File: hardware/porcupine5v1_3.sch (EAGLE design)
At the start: 45 parts, among them X1 PROGCON

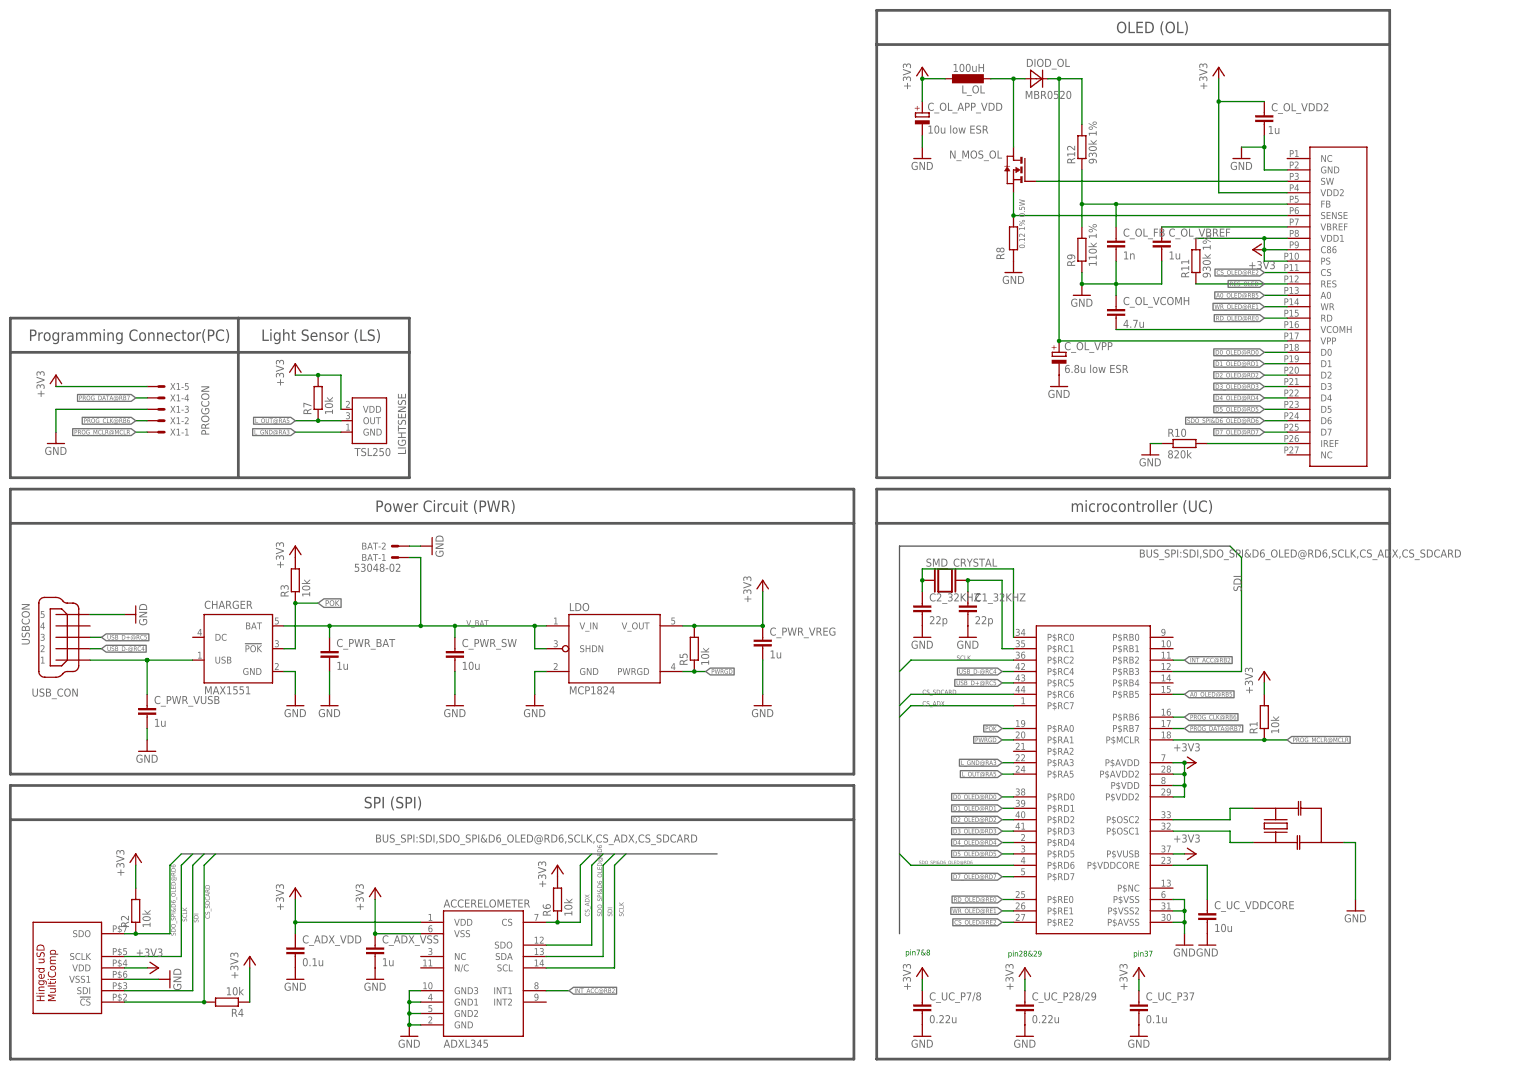
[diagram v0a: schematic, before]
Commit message: OLED version update wiring
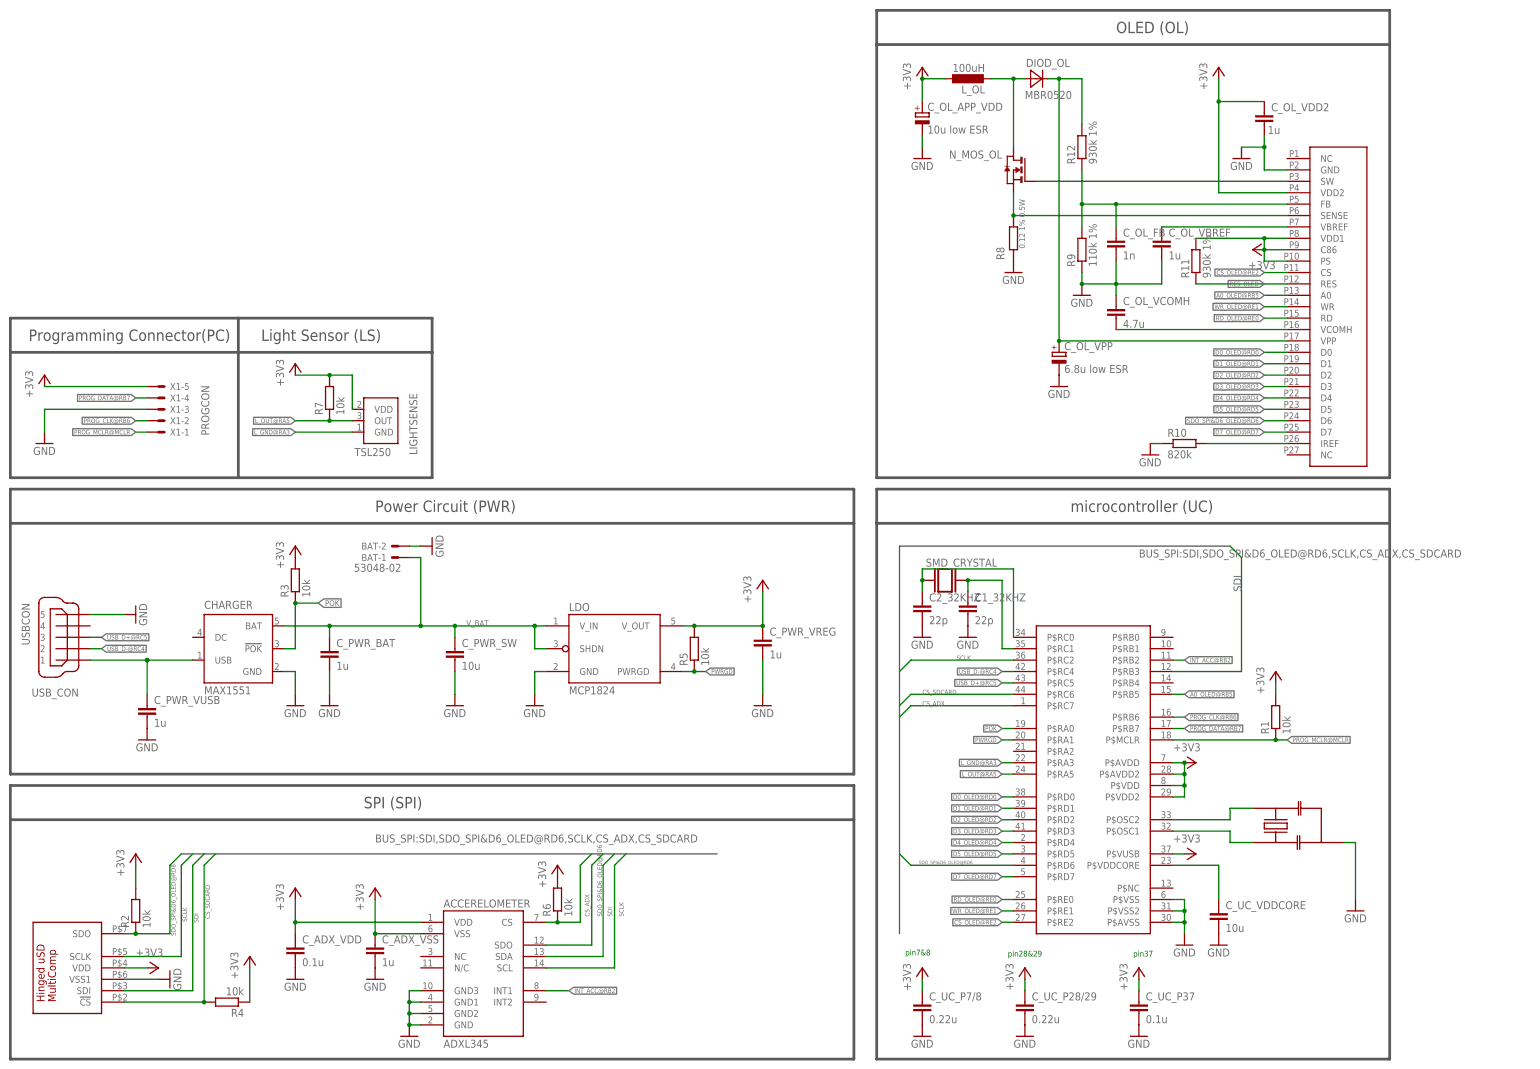
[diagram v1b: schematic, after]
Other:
- moved on the sheet: C_UC_VDDCORE, LIGHTSENSE, R1, R7
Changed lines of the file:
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@@
 <wire x1="5.08" y1="132.08" x2="55.88" y2="132.08" width="0.6096" layer="97"/>
 <wire x1="55.88" y1="167.64" x2="5.08" y2="167.64" width="0.6096" layer="97"/>
-<wire x1="55.88" y1="132.08" x2="93.98" y2="132.08" width="0.6096" layer="97"/>
-<wire x1="93.98" y1="132.08" x2="93.98" y2="160.02" width="0.6096" layer="97"/>
-<wire x1="93.98" y1="160.02" x2="93.98" y2="167.64" width="0.6096" layer="97"/>
+<wire x1="55.88" y1="132.08" x2="99.06" y2="132.08" width="0.6096" layer="97"/>
+<wire x1="99.06" y1="132.08" x2="99.06" y2="160.02" width="0.6096" layer="97"/>
+<wire x1="99.06" y1="160.02" x2="99.06" y2="167.64" width="0.6096" layer="97"/>
 <wire x1="55.88" y1="167.64" x2="55.88" y2="132.08" width="0.6096" layer="97"/>
 <wire x1="5.08" y1="121.92" x2="5.08" y2="66.04" width="0.6096" layer="97"/>
@@
 <wire x1="312.42" y1="121.92" x2="312.42" y2="2.54" width="0.6096" layer="97"/>
 <wire x1="312.42" y1="2.54" x2="198.12" y2="2.54" width="0.6096" layer="97"/>
-<wire x1="5.08" y1="160.02" x2="93.98" y2="160.02" width="0.6096" layer="97"/>
-<wire x1="55.88" y1="167.64" x2="93.98" y2="167.64" width="0.6096" layer="97"/>
+<wire x1="5.08" y1="160.02" x2="99.06" y2="160.02" width="0.6096" layer="97"/>
+<wire x1="55.88" y1="167.64" x2="99.06" y2="167.64" width="0.6096" layer="97"/>
 <text x="9.144" y="162.56" size="2.54" layer="97">Programming Connector(PC)</text>
 <text x="204.47" y="25.654" size="1.27" layer="91">pin7&amp;8</text>
@@
 </plain>
 <instances>
-<instance part="GND3" gate="1" x="15.24" y="139.7"/>
+<instance part="GND3" gate="1" x="12.7" y="139.7"/>
 <instance part="SDCARD_CON" gate="G$1" x="30.48" y="25.4" smashed="yes" rot="R90"/>
 <instance part="GND16" gate="1" x="40.64" y="20.32" rot="R90"/>
-<instance part="LIGHTSENSE" gate="G$1" x="88.9" y="137.16" smashed="yes">
-<attribute name="NAME" x="93.218" y="137.16" size="1.778" layer="95" rot="R90"/>
+<instance part="LIGHTSENSE" gate="G$1" x="91.44" y="137.16" smashed="yes">
+<attribute name="NAME" x="95.758" y="137.16" size="1.778" layer="95" rot="R90"/>
 <attribute name="VALUE" x="89.916" y="138.684" size="1.778" layer="96" rot="R180"/>
 </instance>
@@
 <instance part="GND20" gate="1" x="33.02" y="101.6" rot="R90"/>
 <instance part="C_PWR_VUSB" gate="G$1" x="35.56" y="81.28"/>
-<instance part="GND21" gate="1" x="35.56" y="71.12"/>
+<instance part="GND21" gate="1" x="35.56" y="73.66"/>
 <instance part="GND23" gate="1" x="99.06" y="116.84" rot="R90"/>
 <instance part="C_PWR_SW" gate="G$1" x="104.14" y="93.98"/>
@@
 <instance part="+3V7" gate="G$1" x="269.24" y="68.58" rot="R270"/>
 <instance part="GND6" gate="1" x="266.7" y="27.94"/>
-<instance part="GND7" gate="1" x="271.78" y="27.94"/>
+<instance part="GND7" gate="1" x="274.32" y="27.94"/>
 <instance part="C_UC_P7/8" gate="G$1" x="208.28" y="15.24"/>
 <instance part="C_UC_P28/29" gate="G$1" x="231.14" y="15.24"/>
@@
 <instance part="GND13" gate="1" x="208.28" y="7.62"/>
 <instance part="+3V14" gate="G$1" x="68.58" y="157.48"/>
-<instance part="R1" gate="G$1" x="284.48" y="78.74" rot="R90"/>
-<instance part="+3V15" gate="G$1" x="15.24" y="154.94"/>
+<instance part="R1" gate="G$1" x="287.02" y="78.74" rot="R90"/>
+<instance part="+3V15" gate="G$1" x="12.7" y="154.94"/>
 <instance part="+3V13" gate="G$1" x="86.36" y="40.64"/>
-<instance part="+3V16" gate="G$1" x="284.48" y="88.9"/>
+<instance part="+3V16" gate="G$1" x="287.02" y="88.9"/>
 <instance part="R2" gate="G$1" x="33.02" y="35.56" rot="R90"/>
 <instance part="R4" gate="G$1" x="53.34" y="15.24" rot="R180"/>
 <instance part="+3V8" gate="G$1" x="33.02" y="48.26"/>
 <instance part="+3V10" gate="G$1" x="58.42" y="25.4"/>
-<instance part="C_UC_VDDCORE" gate="G$1" x="271.78" y="35.56"/>
+<instance part="C_UC_VDDCORE" gate="G$1" x="274.32" y="35.56"/>
 <instance part="+3V2" gate="G$1" x="38.1" y="22.86" rot="R270"/>
 <instance part="CON_OLED" gate="G$1" x="292.1" y="170.18"/>
@@
 <instance part="BAT" gate="-1" x="91.44" y="114.3" rot="R180"/>
 <instance part="BAT" gate="-2" x="91.44" y="116.84" rot="R180"/>
-<instance part="R7" gate="G$1" x="73.66" y="149.86" rot="R90"/>
+<instance part="R7" gate="G$1" x="76.2" y="149.86" rot="R90"/>
 </instances>
 <busses>
@@
 <net name="GND" class="0">
 <segment>
-<wire x1="35.56" y1="147.32" x2="15.24" y2="147.32" width="0.1524" layer="91"/>
-<wire x1="15.24" y1="147.32" x2="15.24" y2="142.24" width="0.1524" layer="91"/>
+<wire x1="35.56" y1="147.32" x2="12.7" y2="147.32" width="0.1524" layer="91"/>
+<wire x1="12.7" y1="147.32" x2="12.7" y2="142.24" width="0.1524" layer="91"/>
 <pinref part="GND3" gate="1" pin="GND"/>
 <pinref part="X1" gate="-3" pin="S"/>
@@
 </segment>
 <segment>
-<wire x1="35.56" y1="76.2" x2="35.56" y2="73.66" width="0.1524" layer="91"/>
 <pinref part="C_PWR_VUSB" gate="G$1" pin="2"/>
 <pinref part="GND21" gate="1" pin="GND"/>
@@
 <pinref part="LIGHTSENSE" gate="G$1" pin="OUT"/>
 <pinref part="R7" gate="G$1" pin="1"/>
-<wire x1="73.66" y1="144.78" x2="68.58" y2="144.78" width="0.1524" layer="91"/>
-<wire x1="78.74" y1="144.78" x2="73.66" y2="144.78" width="0.1524" layer="91"/>
-<junction x="73.66" y="144.78"/>
+<wire x1="76.2" y1="144.78" x2="68.58" y2="144.78" width="0.1524" layer="91"/>
+<wire x1="81.28" y1="144.78" x2="76.2" y2="144.78" width="0.1524" layer="91"/>
+<junction x="76.2" y="144.78"/>
 </segment>
 <segment>
@@
 </segment>
 <segment>
-<wire x1="68.58" y1="154.94" x2="73.66" y2="154.94" width="0.1524" layer="91"/>
-<wire x1="73.66" y1="154.94" x2="78.74" y2="154.94" width="0.1524" layer="91"/>
-<wire x1="78.74" y1="154.94" x2="78.74" y2="147.32" width="0.1524" layer="91"/>
+<wire x1="68.58" y1="154.94" x2="76.2" y2="154.94" width="0.1524" layer="91"/>
+<wire x1="76.2" y1="154.94" x2="81.28" y2="154.94" width="0.1524" layer="91"/>
+<wire x1="81.28" y1="154.94" x2="81.28" y2="147.32" width="0.1524" layer="91"/>
 <pinref part="LIGHTSENSE" gate="G$1" pin="VDD"/>
 <pinref part="+3V14" gate="G$1" pin="+3V3"/>
 <pinref part="R7" gate="G$1" pin="2"/>
-<junction x="73.66" y="154.94"/>
-</segment>
-<segment>
-<wire x1="35.56" y1="152.4" x2="15.24" y2="152.4" width="0.1524" layer="91"/>
+<junction x="76.2" y="154.94"/>
+</segment>
+<segment>
+<wire x1="35.56" y1="152.4" x2="12.7" y2="152.4" width="0.1524" layer="91"/>
 <pinref part="+3V15" gate="G$1" pin="+3V3"/>
 <pinref part="X1" gate="-5" pin="S"/>
@@
 </segment>
 <segment>
-<wire x1="284.48" y1="83.82" x2="284.48" y2="86.36" width="0.1524" layer="91"/>
+<wire x1="287.02" y1="83.82" x2="287.02" y2="86.36" width="0.1524" layer="91"/>
 <pinref part="R1" gate="G$1" pin="2"/>
 <pinref part="+3V16" gate="G$1" pin="+3V3"/>
@@
 <net name="VDDCORE" class="0">
 <segment>
-<wire x1="271.78" y1="38.1" x2="271.78" y2="45.72" width="0.1524" layer="91"/>
-<wire x1="271.78" y1="45.72" x2="264.16" y2="45.72" width="0.1524" layer="91"/>
+<wire x1="274.32" y1="38.1" x2="274.32" y2="45.72" width="0.1524" layer="91"/>
+<wire x1="274.32" y1="45.72" x2="264.16" y2="45.72" width="0.1524" layer="91"/>
 <pinref part="PIC_CONTROLLER" gate="G$1" pin="P$VDDCORE"/>
 <pinref part="C_UC_VDDCORE" gate="G$1" pin="1"/>
@@
 <net name="PROG_MCLR@MCLR" class="0">
 <segment>
-<wire x1="264.16" y1="73.66" x2="284.48" y2="73.66" width="0.1524" layer="91"/>
-<wire x1="289.56" y1="73.66" x2="284.48" y2="73.66" width="0.1524" layer="91"/>
-<junction x="284.48" y="73.66"/>
+<wire x1="264.16" y1="73.66" x2="287.02" y2="73.66" width="0.1524" layer="91"/>
+<wire x1="289.56" y1="73.66" x2="287.02" y2="73.66" width="0.1524" layer="91"/>
+<junction x="287.02" y="73.66"/>
 <label x="289.56" y="73.66" size="1.016" layer="95" xref="yes"/>
 <pinref part="PIC_CONTROLLER" gate="G$1" pin="P$MCLR"/>
@@
 <segment>
 <pinref part="LIGHTSENSE" gate="G$1" pin="GND"/>
-<wire x1="78.74" y1="142.24" x2="68.58" y2="142.24" width="0.1524" layer="91"/>
+<wire x1="81.28" y1="142.24" x2="68.58" y2="142.24" width="0.1524" layer="91"/>
 <label x="68.58" y="142.24" size="1.016" layer="95" rot="R180" xref="yes"/>
 </segment>
@@
 </sheet>
 </sheets>
+<errors>
+</errors>
 </schematic>
 </drawing>

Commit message: OLED version: update wiring, added layout docs
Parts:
- renumbered U$2 to SMD_CRYSTAL, U$3 to RESONATOR
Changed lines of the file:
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@@
 <part name="R5" library="rcl" deviceset="R-EU_" device="R0603" value="10k"/>
 <part name="+3V20" library="supply1" deviceset="+3V3" device=""/>
-<part name="U$2" library="HedgehogLib" deviceset="SMD_CRYSTAL" device=""/>
-<part name="U$3" library="jnode" deviceset="RESONATOR" device="PRQC-S"/>
+<part name="SMD_CRYSTAL" library="HedgehogLib" deviceset="SMD_CRYSTAL" device=""/>
+<part name="RESONATOR" library="jnode" deviceset="RESONATOR" device="PRQC-S"/>
 <part name="GND17" library="supply1" deviceset="GND" device=""/>
 <part name="BAT" library="con-molex" deviceset="53?-02" device="048"/>
@@
 <instance part="R5" gate="G$1" x="157.48" y="93.98" rot="R90"/>
 <instance part="+3V20" gate="G$1" x="68.58" y="116.84"/>
-<instance part="U$2" gate="G$1" x="213.36" y="109.22"/>
-<instance part="U$3" gate="G$1" x="289.56" y="53.34" rot="R180"/>
+<instance part="SMD_CRYSTAL" gate="G$1" x="213.36" y="109.22"/>
+<instance part="RESONATOR" gate="G$1" x="289.56" y="53.34" rot="R180"/>
 <instance part="GND17" gate="1" x="76.2" y="81.28"/>
 <instance part="BAT" gate="-1" x="91.44" y="114.3" rot="R180"/>
@@
 <segment>
 <pinref part="GND2" gate="1" pin="GND"/>
-<pinref part="U$3" gate="G$1" pin="GND"/>
+<pinref part="RESONATOR" gate="G$1" pin="GND"/>
 <wire x1="302.26" y1="50.8" x2="304.8" y2="50.8" width="0.1524" layer="91"/>
 <wire x1="304.8" y1="50.8" x2="304.8" y2="38.1" width="0.1524" layer="91"/>
@@
 <pinref part="C2_32KHZ" gate="G$1" pin="1"/>
 <pinref part="PIC_CONTROLLER" gate="G$1" pin="P$RC0"/>
-<pinref part="U$2" gate="G$1" pin="1"/>
+<pinref part="SMD_CRYSTAL" gate="G$1" pin="1"/>
 <junction x="208.28" y="109.22"/>
 <wire x1="208.28" y1="109.22" x2="208.28" y2="106.68" width="0.1524" layer="91"/>
@@
 <pinref part="C1_32KHZ" gate="G$1" pin="1"/>
 <pinref part="PIC_CONTROLLER" gate="G$1" pin="P$RC1"/>
-<pinref part="U$2" gate="G$1" pin="2"/>
+<pinref part="SMD_CRYSTAL" gate="G$1" pin="2"/>
 <junction x="218.44" y="109.22"/>
 <wire x1="218.44" y1="109.22" x2="218.44" y2="106.68" width="0.1524" layer="91"/>
@@
 <wire x1="264.16" y1="55.88" x2="276.86" y2="55.88" width="0.1524" layer="91"/>
 <wire x1="276.86" y1="55.88" x2="276.86" y2="58.42" width="0.1524" layer="91"/>
-<pinref part="U$3" gate="G$1" pin="1"/>
+<pinref part="RESONATOR" gate="G$1" pin="1"/>
 <wire x1="276.86" y1="58.42" x2="281.94" y2="58.42" width="0.1524" layer="91"/>
 </segment>
@@
 <net name="N$2" class="0">
 <segment>
-<pinref part="U$3" gate="G$1" pin="2"/>
+<pinref part="RESONATOR" gate="G$1" pin="2"/>
 <wire x1="281.94" y1="50.8" x2="276.86" y2="50.8" width="0.1524" layer="91"/>
 <wire x1="276.86" y1="50.8" x2="276.86" y2="53.34" width="0.1524" layer="91"/>
